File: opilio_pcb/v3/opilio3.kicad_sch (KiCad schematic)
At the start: 90 parts, among them J1 Screw_Terminal_01x02, J2 Conn_01x02_Male, J3 USB_B_Micro, J4 Program, Q1 HSBA3048, Q2 HSBA3048, U1 EUP3458, U2 SCT51240, U3 SCT51240, U4 USBLC6-2SC6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

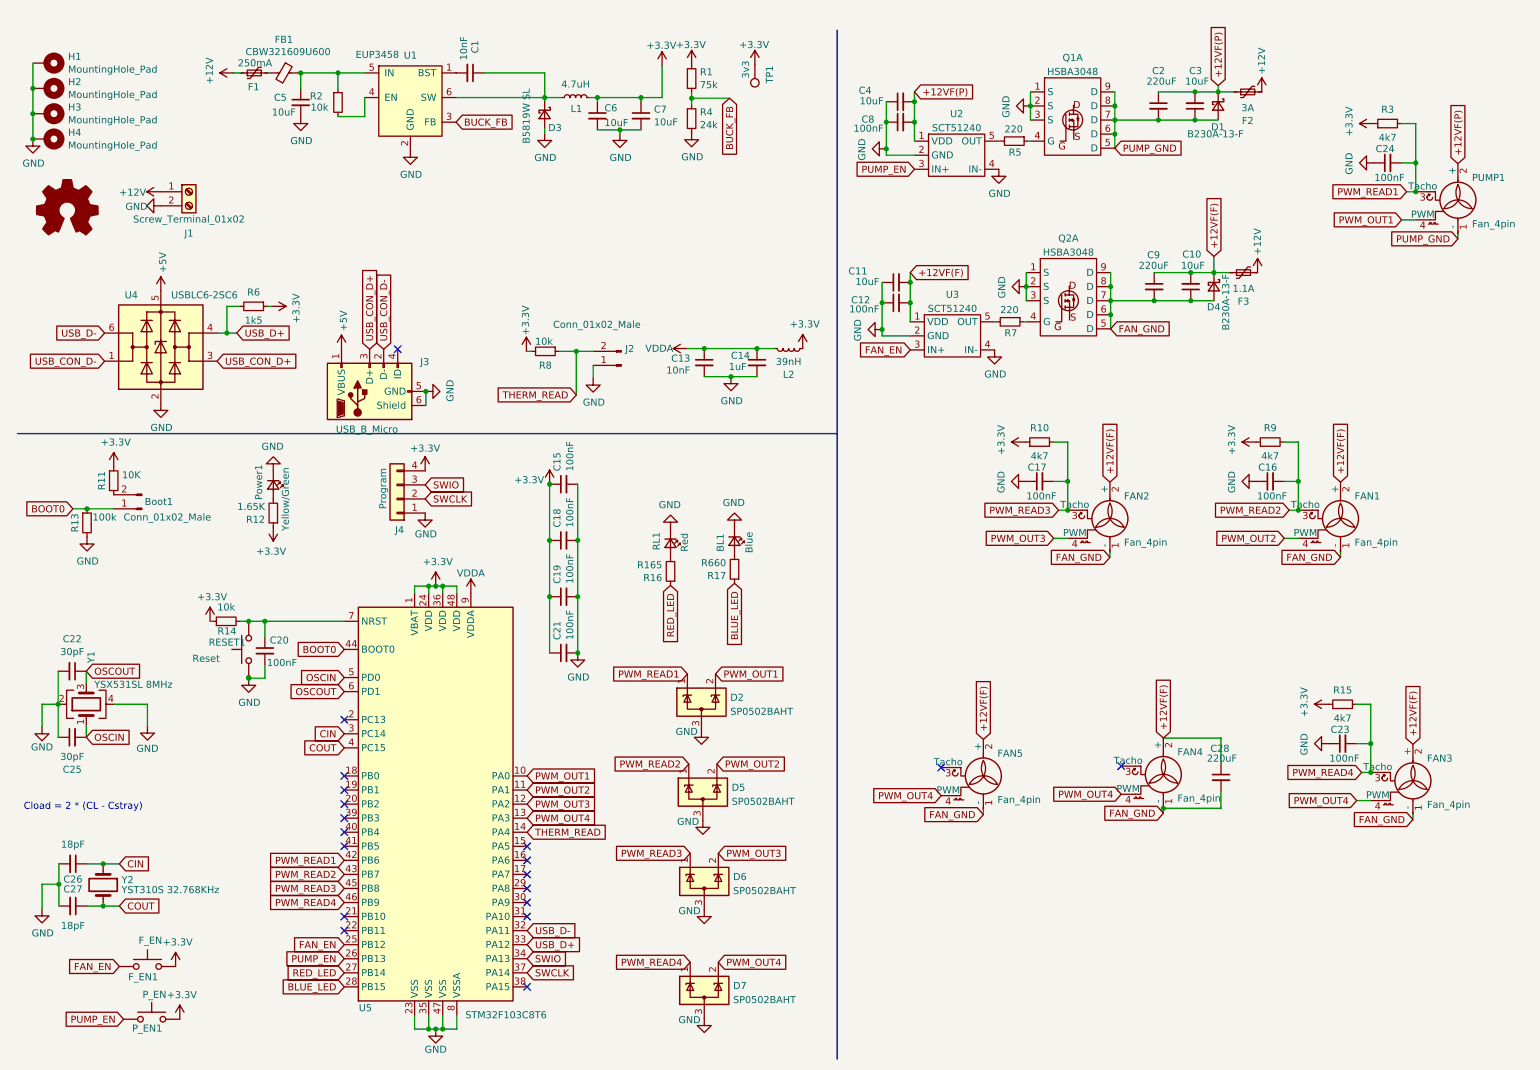
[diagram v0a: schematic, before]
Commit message: Board updated to v3.1 (#7)
* refactor to updated shared lib

* stabalize temp reading by averaging

* stabalize temp reading by averaging

* move schematice tiny bit

* add power flag

* common

* save standby

* move duty calculation to config, prep for fan curve

* update pcb

* set led high if thermister value is too low

* deal with entire config

* add pcb v3.1

* moved opilio 3.1

* almost ready for v3.1

* add ambient temprature to stats

* uploading config works

* opt 3
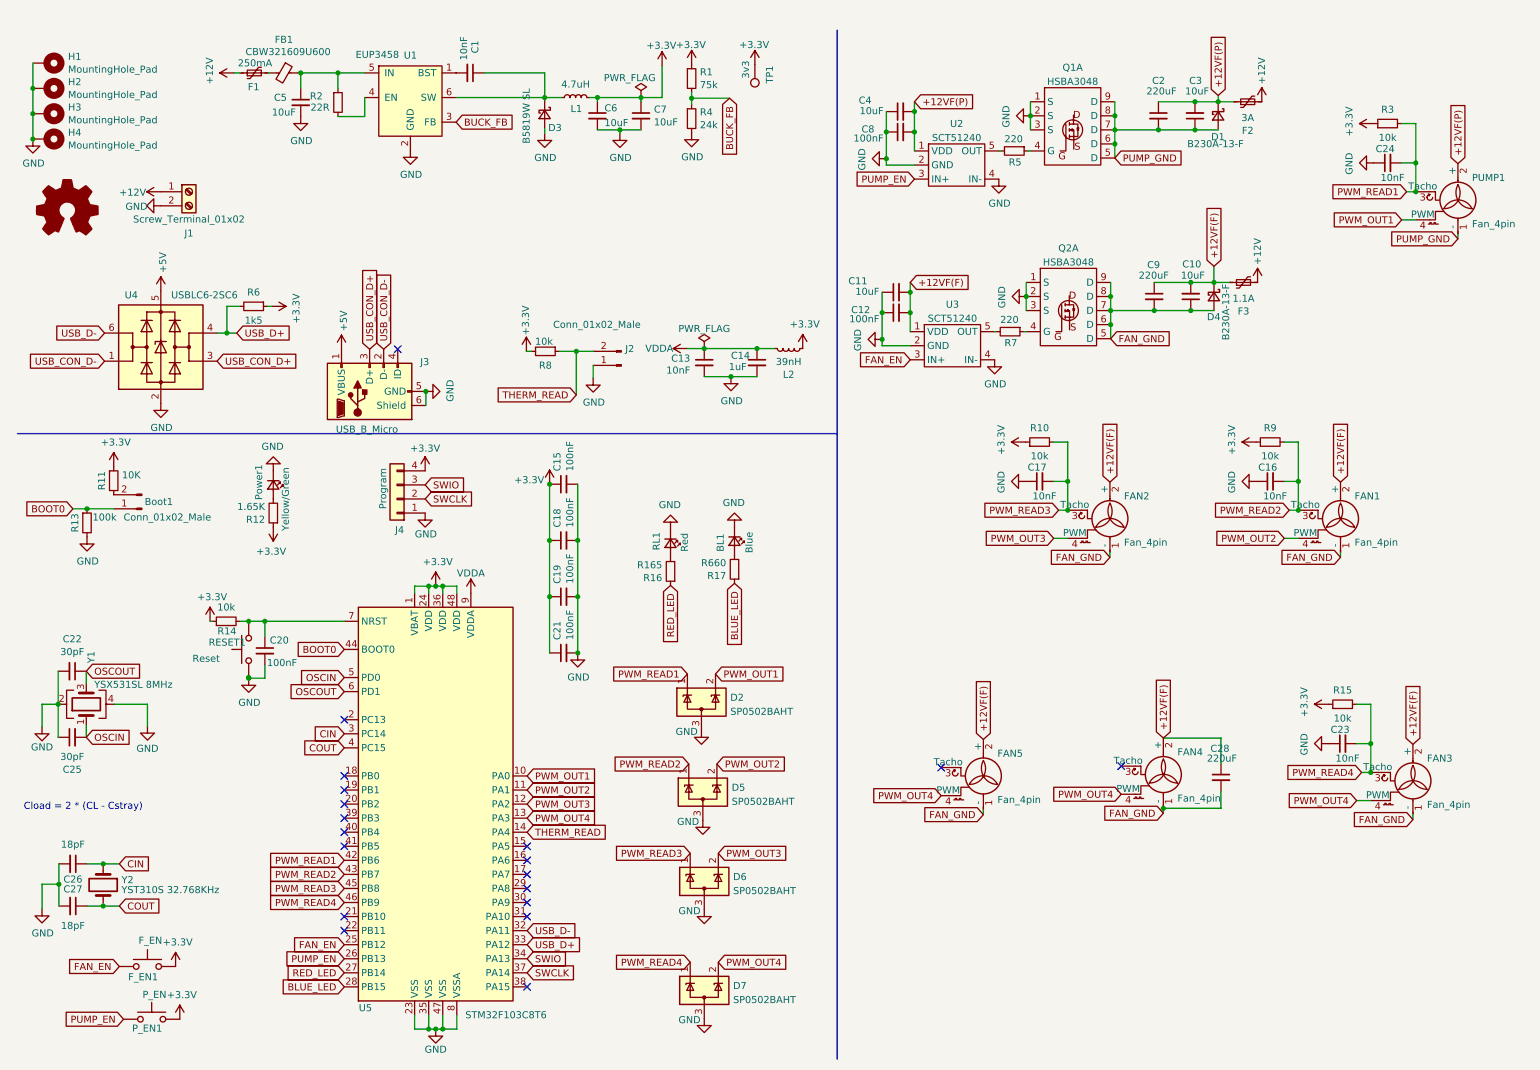
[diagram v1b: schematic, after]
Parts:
- C16, C17, C23, C24: value 100nF -> 10nF
- R10, R15, R3, R9: value 4k7 -> 10k
- R2: value 10k -> 22R
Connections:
- net +3V3 renamed +3.3V
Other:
- moved on the sheet: C10, C11, C12, C2, C3, C4, C8, C9, D1, D4, F2, F3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
